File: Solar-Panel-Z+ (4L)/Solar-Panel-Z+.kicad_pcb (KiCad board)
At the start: 4 copper layers, 48.4 x 48.4 mm, 79 parts, among them J1 FTS-105-01-L-DV-A, Q1 BSS138DWQ-7, Q2 MBT2222ADW1T1, Q3 BSS138DWQ-7, Q4 MBT2222ADW1T1, U1 BQ25570RGRR, U2 TSL2561

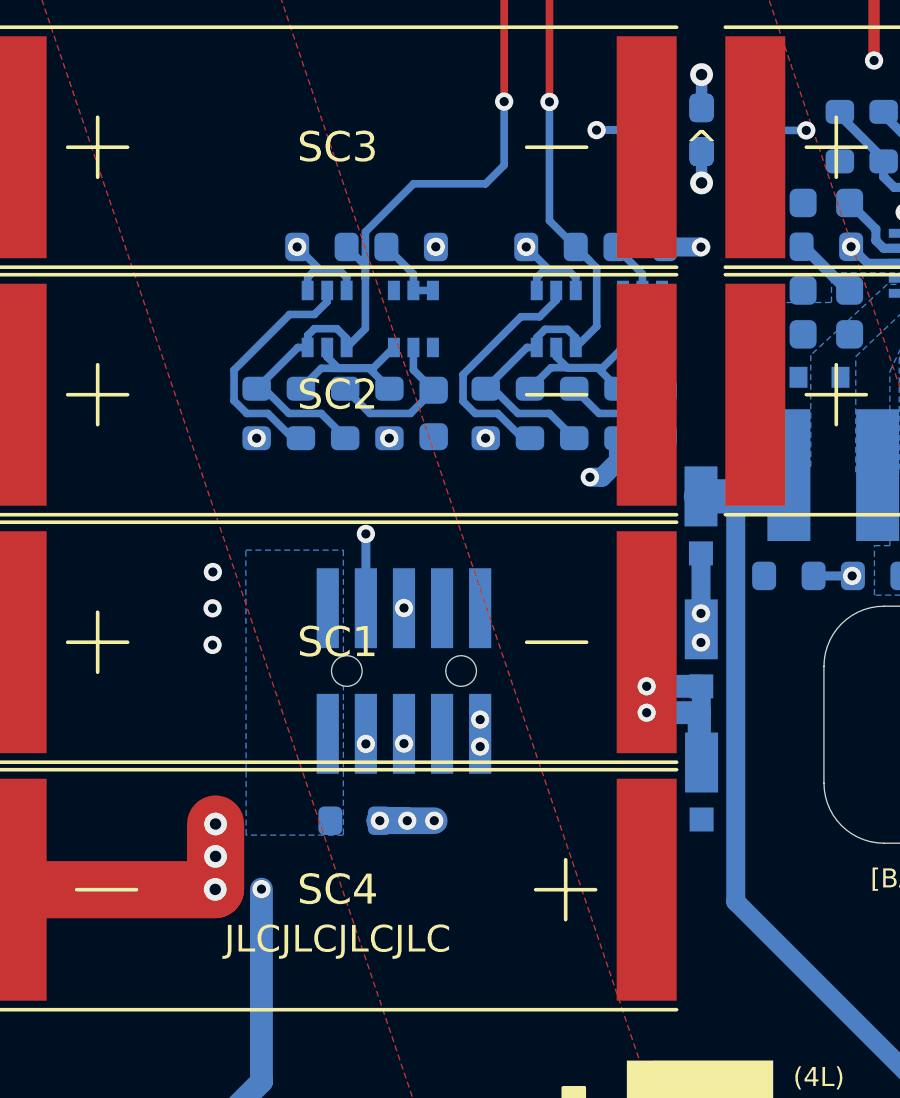
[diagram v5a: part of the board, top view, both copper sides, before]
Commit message: DFM updates and repositioned -Z mounting holes
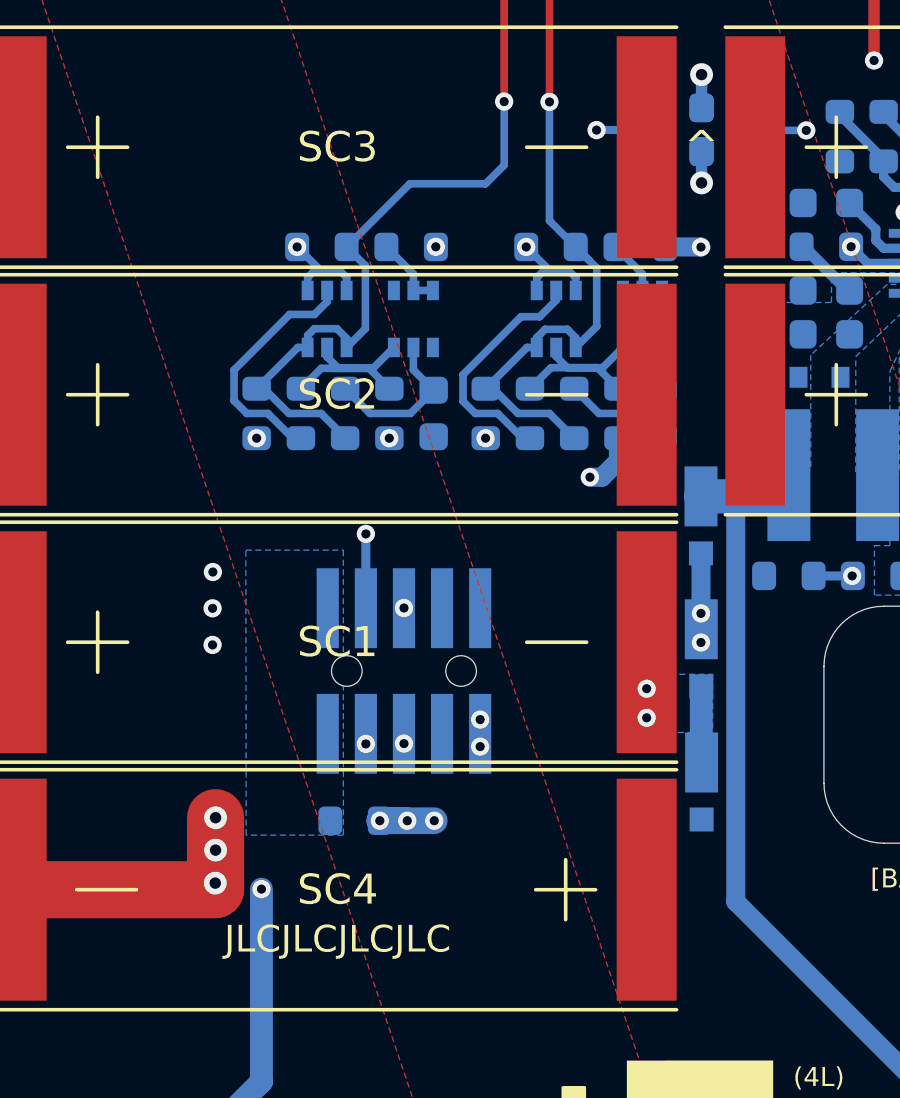
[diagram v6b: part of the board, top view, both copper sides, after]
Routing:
- net Net-(D3-Pad1): track 6.71 -> 2.54 mm
- net SCL_LS: track 32.0 -> 31.3 mm
- added copper zone on B.Cu, net Net-(D3-Pad1)
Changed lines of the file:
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@@
     (style (thickness 0.1) (arrow_length 1.27) (text_position_mode 0) (extension_height 0.58642) (extension_offset 0.5) keep_text_aligned)
   )
-  (segment (start 90.51 78.64) (end 90.52 78.63) (width 1.905) (layer "F.Cu") (net 1))
   (segment (start 108.22 44.89) (end 108.45 45.12) (width 0.381) (layer "F.Cu") (net 1))
   (segment (start 113.76 46.8056) (end 113.76 51.01) (width 0.381) (layer "F.Cu") (net 1))
-  (segment (start 90.52 78.63) (end 90.52 76.46) (width 1.905) (layer "F.Cu") (net 1))
+  (segment (start 90.52 78.63) (end 90.52 76.25) (width 1.905) (layer "F.Cu") (net 1))
+  (segment (start 90.51 78.64) (end 90.52 78.63) (width 1.905) (layer "F.Cu") (net 1))
   (segment (start 108.45 45.12) (end 112.0744 45.12) (width 0.381) (layer "F.Cu") (net 1))
   (segment (start 112.0744 45.12) (end 113.76 46.8056) (width 0.381) (layer "F.Cu") (net 1))
@@
   (via (at 113.76 51.01) (size 0.6096) (drill 0.3048) (layers "F.Cu" "B.Cu") (net 1))
   (via (at 123.12 60.14) (size 0.6096) (drill 0.3048) (layers "F.Cu" "B.Cu") (net 1))
-  (via (at 90.51 78.64) (size 0.762) (drill 0.381) (layers "F.Cu" "B.Cu") (net 1))
+  (via (at 90.51 78.43) (size 0.762) (drill 0.381) (layers "F.Cu" "B.Cu") (net 1))
   (via (at 123.12 58.7) (size 0.6096) (drill 0.3048) (layers "F.Cu" "B.Cu") (net 1))
-  (via (at 90.52 77.54) (size 0.762) (drill 0.381) (layers "F.Cu" "B.Cu") (net 1))
-  (via (at 90.52 76.46) (size 0.762) (drill 0.381) (layers "F.Cu" "B.Cu") (net 1))
+  (via (at 90.52 77.33) (size 0.762) (drill 0.381) (layers "F.Cu" "B.Cu") (net 1))
+  (via (at 90.52 76.25) (size 0.762) (drill 0.381) (layers "F.Cu" "B.Cu") (net 1))
   (via (at 123.12 55.9) (size 0.6096) (drill 0.3048) (layers "F.Cu" "B.Cu") (free) (net 1))
   (via (at 123.12 57.22) (size 0.6096) (drill 0.3048) (layers "F.Cu" "B.Cu") (net 1))
@@
   (segment (start 102.475 61.95) (end 103.3 62.775) (width 0.254) (layer "B.Cu") (net 24))
   (segment (start 105.425 62) (end 104.75 61.325) (width 0.254) (layer "B.Cu") (net 24))
-  (via (at 104.89 71.87) (size 0.6096) (drill 0.3048) (layers "F.Cu" "B.Cu") (net 25))
-  (via (at 104.89 72.75) (size 0.6096) (drill 0.3048) (layers "F.Cu" "B.Cu") (net 25))
-  (segment (start 106.71 71.87) (end 106.71 72.68) (width 0.635) (layer "B.Cu") (net 25))
-  (segment (start 106.71 72.68) (end 106.71 74.4) (width 0.635) (layer "B.Cu") (net 25))
-  (segment (start 104.89 72.75) (end 106.58 72.75) (width 0.762) (layer "B.Cu") (net 25))
-  (segment (start 106.64 72.81) (end 106.64 73.4) (width 0.762) (layer "B.Cu") (net 25))
-  (segment (start 106.58 72.75) (end 106.64 72.81) (width 0.762) (layer "B.Cu") (net 25))
-  (segment (start 104.89 71.87) (end 106.71 71.87) (width 0.762) (layer "B.Cu") (net 25))
+  (via (at 104.89 71.95) (size 0.6096) (drill 0.3048) (layers "F.Cu" "B.Cu") (net 25))
+  (via (at 104.89 72.92) (size 0.6096) (drill 0.3048) (layers "F.Cu" "B.Cu") (net 25))
+  (segment (start 106.71 71.87) (end 106.71 74.4) (width 0.762) (layer "B.Cu") (net 25))
+  (segment (start 106.71 74.4) (end 106.72 74.41) (width 0.762) (layer "B.Cu") (net 25))
   (segment (start 97.1147 58.675) (end 97.7647 58.675) (width 0.254) (layer "B.Cu") (net 26))
   (segment (start 97.1147 58.125) (end 96.2147 57.225) (width 0.254) (layer "B.Cu") (net 26))
@@
   (via (at 100.14 52.38) (size 0.6096) (drill 0.3048) (layers "F.Cu" "B.Cu") (net 29))
   (segment (start 94.8897 60.275) (end 94.8897 60.575) (width 0.254) (layer "B.Cu") (net 29))
-  (segment (start 97.12 55.12) (end 95.5147 56.7253) (width 0.254) (layer "B.Cu") (net 29))
-  (segment (start 95.5147 56.7253) (end 95.5147 58.2747) (width 0.254) (layer "B.Cu") (net 29))
   (segment (start 94.8897 57.225) (end 95.5147 57.85) (width 0.254) (layer "B.Cu") (net 29))
+  (segment (start 100.14 52.38) (end 100.14 54.5) (width 0.254) (layer "B.Cu") (net 29))
   (segment (start 93.5897 60.575) (end 93.2647 60.575) (width 0.254) (layer "B.Cu") (net 29))
-  (segment (start 95.5147 58.2747) (end 95.5147 59.95) (width 0.254) (layer "B.Cu") (net 29))
   (segment (start 92.1397 61.95) (end 92.9647 62.775) (width 0.254) (layer "B.Cu") (net 29))
   (segment (start 93.8147 59.95) (end 94.5647 59.95) (width 0.254) (layer "B.Cu") (net 29))
+  (segment (start 100.14 54.5) (end 99.52 55.12) (width 0.254) (layer "B.Cu") (net 29))
+  (segment (start 95.5147 59.95) (end 94.8897 60.575) (width 0.254) (layer "B.Cu") (net 29))
+  (segment (start 96.9947 55.12) (end 94.8897 57.225) (width 0.254) (layer "B.Cu") (net 29))
   (segment (start 93.2647 60.575) (end 91.8897 61.95) (width 0.254) (layer "B.Cu") (net 29))
   (segment (start 94.0397 62.775) (end 94.8397 63.575) (width 0.254) (layer "B.Cu") (net 29))
   (segment (start 94.5647 59.95) (end 94.8897 60.275) (width 0.254) (layer "B.Cu") (net 29))
   (segment (start 93.5897 60.175) (end 93.8147 59.95) (width 0.254) (layer "B.Cu") (net 29))
-  (segment (start 95.5147 59.95) (end 94.8897 60.575) (width 0.254) (layer "B.Cu") (net 29))
-  (segment (start 95.5147 57.85) (end 95.5147 58.2747) (width 0.254) (layer "B.Cu") (net 29))
-  (segment (start 100.14 54.5) (end 99.52 55.12) (width 0.254) (layer "B.Cu") (net 29))
+  (segment (start 99.52 55.12) (end 96.9947 55.12) (width 0.254) (layer "B.Cu") (net 29))
   (segment (start 92.9647 62.775) (end 94.0397 62.775) (width 0.254) (layer "B.Cu") (net 29))
+  (segment (start 95.5147 57.85) (end 95.5147 59.95) (width 0.254) (layer "B.Cu") (net 29))
   (segment (start 93.5897 60.575) (end 93.5897 60.175) (width 0.254) (layer "B.Cu") (net 29))
-  (segment (start 100.14 52.38) (end 100.14 54.5) (width 0.254) (layer "B.Cu") (net 29))
-  (segment (start 99.52 55.12) (end 97.12 55.12) (width 0.254) (layer "B.Cu") (net 29))
   (segment (start 104.75 58.675) (end 104.75 58.125) (width 0.254) (layer "B.Cu") (net 30))
   (segment (start 104.75 58.125) (end 103.85 57.225) (width 0.254) (layer "B.Cu") (net 30))
@@
       )
     )
+  )
+  (zone (net 25) (net_name "Net-(D3-Pad1)") (layer "B.Cu") (hatch edge 0.508)
+    (priority 1)
+    (connect_pads yes (clearance 0.1524))
+    (min_thickness 0.254) (filled_areas_thickness no)
+    (fill yes (thermal_gap 0.508) (thermal_bridge_width 0.508))
+    (polygon
+      (pts
+        (xy 107.09 73.41)
+        (xy 104.38 73.41)
+        (xy 104.38 71.47)
+        (xy 107.09 71.47)
+      )
+    )
